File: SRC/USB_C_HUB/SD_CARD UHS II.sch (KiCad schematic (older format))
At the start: 20 parts, among them IC3 USB2240-AEZG-06, J8 SD_Card, Y6 24.0MHz

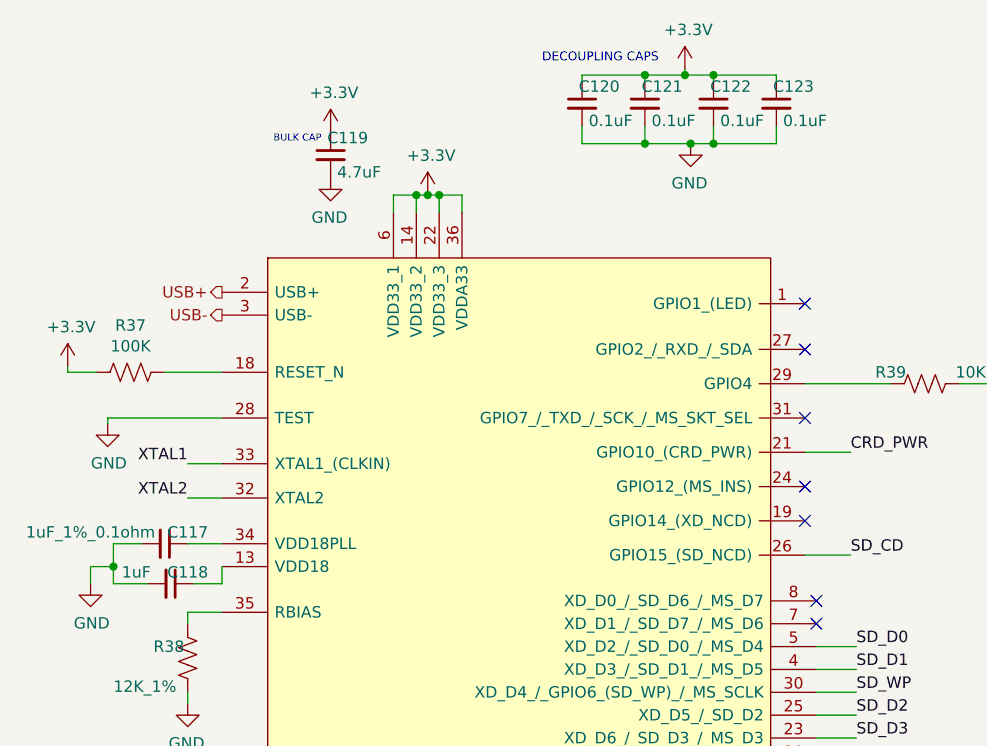
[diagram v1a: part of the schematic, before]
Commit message: schematic capture and footprint assignment complete. Pending approval
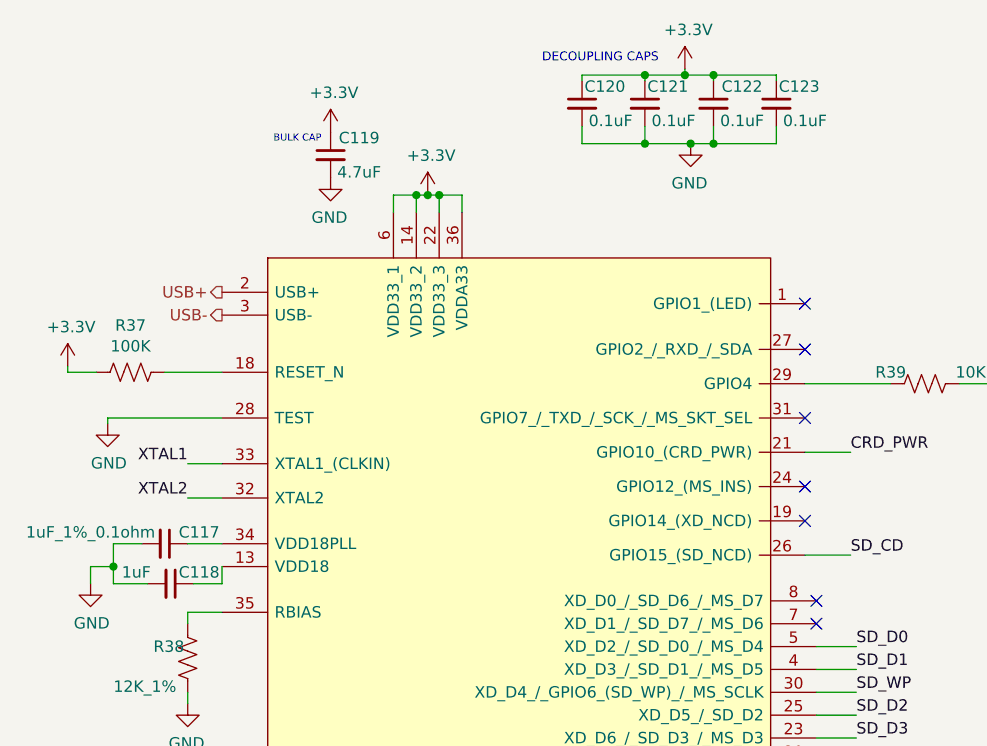
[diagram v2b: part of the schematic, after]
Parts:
- C115, C116: footprint (none) -> Capacitor_SMD:C_0402_1005Metric; Mfr No. (none) -> 0402CG180J500NT
- C117, C118: footprint (none) -> Capacitor_SMD:C_0603_1608Metric; Mfr No. (none) -> GMC10X7R105J16NT
- C119: footprint (none) -> Capacitor_SMD:C_0603_1608Metric; Mfr No. (none) -> CL10A475KQ8NNNC
- C120, C121, C122, C123: footprint (none) -> Capacitor_SMD:C_0402_1005Metric
- C124: footprint (none) -> Capacitor_SMD:C_0402_1005Metric; Mfr No (none) -> C0402C102J1GEC7411
- C125: footprint (none) -> Capacitor_SMD:C_0603_1608Metric
- C126: footprint (none) -> Capacitor_SMD:C_0402_1005Metric; Field4 (none) -> C0402C102J1GEC7411
- J8: footprint (none) -> footprints:3M_SD-RSMT-2-MQ-WF
- R36, R37, R38, R39, R40: footprint (none) -> Resistor_SMD:R_0402_1005Metric
- Y6: footprint (none) -> Crystal:Crystal_SMD_2016-4Pin_2.0x1.6mm; Mfr No. (none) -> ABM11-24.000MHZ-D2X-T3
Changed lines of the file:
@@
 F 0 "C124" H 7892 3621 50  0000 L CNN
 F 1 "1nF" H 7892 3530 50  0000 L CNN
-F 2 "" H 7800 3575 50  0001 C CNN
+F 2 "Capacitor_SMD:C_0402_1005Metric" H 7800 3575 50  0001 C CNN
 F 3 "~" H 7800 3575 50  0001 C CNN
+F 4 "C0402C102J1GEC7411" H 7800 3575 50  0001 C CNN "Mfr No"
 	1    7800 3575
 	1    0    0    -1
@@
 F 0 "J8" H 9650 4190 50  0000 C CNN
 F 1 "SD_Card" H 9650 4099 50  0000 C CNN
-F 2 "" H 9650 3525 50  0001 C CNN
+F 2 "footprints:3M_SD-RSMT-2-MQ-WF" H 9650 3525 50  0001 C CNN
 F 3 "http://portal.fciconnect.com/Comergent//fci/drawing/10067847.pdf" H 9650 3525 50  0001 C CNN
 	1    9650 3525
@@
 F 0 "R40" H 8800 2250 50  0000 C CNN
 F 1 "10K" H 8800 2500 50  0000 C CNN
-F 2 "" V 8940 2365 50  0001 C CNN
+F 2 "Resistor_SMD:R_0402_1005Metric" V 8940 2365 50  0001 C CNN
 F 3 "~" H 8900 2375 50  0001 C CNN
 	1    8900 2375
@@
 F 0 "C126" H 8642 2396 50  0000 L CNN
 F 1 "1nF" H 8642 2305 50  0000 L CNN
-F 2 "" H 8550 2350 50  0001 C CNN
+F 2 "Capacitor_SMD:C_0402_1005Metric" H 8550 2350 50  0001 C CNN
 F 3 "~" H 8550 2350 50  0001 C CNN
+F 4 "C0402C102J1GEC7411" H 8550 2350 50  0001 C CNN "Field4"
 	1    8550 2350
 	1    0    0    -1
@@
 F 0 "C125" H 8217 2396 50  0000 L CNN
 F 1 "4.7uF" H 8217 2305 50  0000 L CNN
-F 2 "" H 8125 2350 50  0001 C CNN
+F 2 "Capacitor_SMD:C_0603_1608Metric" H 8125 2350 50  0001 C CNN
 F 3 "~" H 8125 2350 50  0001 C CNN
 	1    8125 2350
@@
 F 0 "R39" V 6775 2025 50  0000 C CNN
 F 1 "10K" V 6775 2375 50  0000 C CNN
-F 2 "" V 6865 2165 50  0001 C CNN
+F 2 "Resistor_SMD:R_0402_1005Metric" V 6865 2165 50  0001 C CNN
 F 3 "~" H 6825 2175 50  0001 C CNN
 	1    6825 2175
@@
 F 0 "R38" H 3450 3425 50  0000 L CNN
 F 1 "12K_1%" H 3275 3250 50  0000 L CNN
-F 2 "" V 3640 3365 50  0001 C CNN
+F 2 "Resistor_SMD:R_0402_1005Metric" V 3640 3365 50  0001 C CNN
 F 3 "~" H 3600 3375 50  0001 C CNN
 	1    3600 3375
@@
 AR Path="/63D2BAD4/63D3323E" Ref="C119"  Part="1"
 AR Path="/66525694/63D3323E" Ref="C?"  Part="1"
-F 0 "C119" H 4300 1250 50  0000 C CNN
+F 0 "C119" H 4350 1250 50  0000 C CNN
 F 1 "4.7uF" H 4350 1100 50  0000 C CNN
-F 2 "" H 4225 1175 50  0001 C CNN
+F 2 "Capacitor_SMD:C_0603_1608Metric" H 4225 1175 50  0001 C CNN
 F 3 "~" H 4225 1175 50  0001 C CNN
+F 4 "CL10A475KQ8NNNC" H 4225 1175 50  0001 C CNN "Mfr No."
 	1    4225 1175
 	1    0    0    -1
@@
 AR Path="/63D2BAD4/63D33238" Ref="C123"  Part="1"
 AR Path="/66525694/63D33238" Ref="C?"  Part="1"
-F 0 "C123" H 6250 1025 50  0000 C CNN
+F 0 "C123" H 6275 1025 50  0000 C CNN
 F 1 "0.1uF" H 6300 875 50  0000 C CNN
-F 2 "" H 6175 950 50  0001 C CNN
+F 2 "Capacitor_SMD:C_0402_1005Metric" H 6175 950 50  0001 C CNN
 F 3 "~" H 6175 950 50  0001 C CNN
 	1    6175 950
@@
 AR Path="/63D2BAD4/63D33232" Ref="C122"  Part="1"
 AR Path="/66525694/63D33232" Ref="C?"  Part="1"
-F 0 "C122" H 5975 1025 50  0000 C CNN
+F 0 "C122" H 6025 1025 50  0000 C CNN
 F 1 "0.1uF" H 6025 875 50  0000 C CNN
-F 2 "" H 5900 950 50  0001 C CNN
+F 2 "Capacitor_SMD:C_0402_1005Metric" H 5900 950 50  0001 C CNN
 F 3 "~" H 5900 950 50  0001 C CNN
 	1    5900 950
@@
 AR Path="/63D2BAD4/642D7816" Ref="C121"  Part="1"
 AR Path="/66525694/642D7816" Ref="C?"  Part="1"
-F 0 "C121" H 5675 1025 50  0000 C CNN
+F 0 "C121" H 5700 1025 50  0000 C CNN
 F 1 "0.1uF" H 5725 875 50  0000 C CNN
-F 2 "" H 5600 950 50  0001 C CNN
+F 2 "Capacitor_SMD:C_0402_1005Metric" H 5600 950 50  0001 C CNN
 F 3 "~" H 5600 950 50  0001 C CNN
 	1    5600 950
@@
 AR Path="/63D2BAD4/642D7815" Ref="C120"  Part="1"
 AR Path="/66525694/642D7815" Ref="C?"  Part="1"
-F 0 "C120" H 5400 1025 50  0000 C CNN
+F 0 "C120" H 5425 1025 50  0000 C CNN
 F 1 "0.1uF" H 5450 875 50  0000 C CNN
-F 2 "" H 5325 950 50  0001 C CNN
+F 2 "Capacitor_SMD:C_0402_1005Metric" H 5325 950 50  0001 C CNN
 F 3 "~" H 5325 950 50  0001 C CNN
 	1    5325 950
@@
 AR Path="/63D2BAD4/642D7814" Ref="C118"  Part="1"
 AR Path="/66525694/642D7814" Ref="C?"  Part="1"
-F 0 "C118" V 3475 3125 50  0000 C CNN
+F 0 "C118" V 3475 3175 50  0000 C CNN
 F 1 "1uF" V 3475 2900 50  0000 C CNN
-F 2 "" H 3525 3050 50  0001 C CNN
+F 2 "Capacitor_SMD:C_0603_1608Metric" H 3525 3050 50  0001 C CNN
 F 3 "~" H 3525 3050 50  0001 C CNN
+F 4 "GMC10X7R105J16NT" V 3525 3050 50  0001 C CNN "Mfr No."
 	1    3525 3050
 	0    1    1    0
@@
 AR Path="/63D2BAD4/642D7812" Ref="C117"  Part="1"
 AR Path="/66525694/642D7812" Ref="C?"  Part="1"
-F 0 "C117" V 3450 2975 50  0000 C CNN
+F 0 "C117" V 3450 3025 50  0000 C CNN
 F 1 "1uF_1%_0.1ohm" V 3450 2550 50  0000 C CNN
-F 2 "" H 3500 2875 50  0001 C CNN
+F 2 "Capacitor_SMD:C_0603_1608Metric" H 3500 2875 50  0001 C CNN
 F 3 "~" H 3500 2875 50  0001 C CNN
+F 4 "GMC10X7R105J16NT" V 3500 2875 50  0001 C CNN "Mfr No."
 	1    3500 2875
 	0    1    1    0
@@
 F 0 "R37" V 3555 2125 50  0000 C CNN
 F 1 "100K" V 3464 2125 50  0000 C CNN
-F 2 "" V 3390 2115 50  0001 C CNN
+F 2 "Resistor_SMD:R_0402_1005Metric" V 3390 2115 50  0001 C CNN
 F 3 "~" H 3350 2125 50  0001 C CNN
 	1    3350 2125
@@
 F 0 "Y6" V 1775 3850 50  0000 L CNN
 F 1 "24.0MHz" V 1550 3800 50  0000 L CNN
-F 2 "" H 1675 3750 50  0001 C CNN
+F 2 "Crystal:Crystal_SMD_2016-4Pin_2.0x1.6mm" H 1675 3750 50  0001 C CNN
 F 3 "~" H 1675 3750 50  0001 C CNN
+F 4 "ABM11-24.000MHZ-D2X-T3" V 1675 3750 50  0001 C CNN "Mfr No."
 	1    1675 3750
 	0    1    1    0
@@
 F 0 "C116" V 1146 3400 50  0000 C CNN
 F 1 "18pF" V 1237 3400 50  0000 C CNN
-F 2 "" H 1375 3400 50  0001 C CNN
+F 2 "Capacitor_SMD:C_0402_1005Metric" H 1375 3400 50  0001 C CNN
 F 3 "~" H 1375 3400 50  0001 C CNN
+F 4 " 0402CG180J500NT" V 1375 3400 50  0001 C CNN "Mfr No."
 	1    1375 3400
 	0    1    1    0
@@
 F 0 "C115" V 1121 4050 50  0000 C CNN
 F 1 "18pF" V 1212 4050 50  0000 C CNN
-F 2 "" H 1350 4050 50  0001 C CNN
+F 2 "Capacitor_SMD:C_0402_1005Metric" H 1350 4050 50  0001 C CNN
 F 3 "~" H 1350 4050 50  0001 C CNN
+F 4 " 0402CG180J500NT" V 1350 4050 50  0001 C CNN "Mfr No."
 	1    1350 4050
 	0    1    1    0
@@
 F 0 "R36" H 2243 3721 50  0000 L CNN
 F 1 "1M" H 2243 3630 50  0000 L CNN
-F 2 "" V 2215 3665 50  0001 C CNN
+F 2 "Resistor_SMD:R_0402_1005Metric" V 2215 3665 50  0001 C CNN
 F 3 "~" H 2175 3675 50  0001 C CNN
 	1    2175 3675
